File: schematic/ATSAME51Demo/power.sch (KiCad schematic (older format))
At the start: 37 parts, among them IC2 AZ1117IH-3.3TRG1, J1 Barrel_Jack_Switch, J2 Power, J3 Conn_01x02, J4 USB_B_Micro, J5 USB_B_Mini, J6 Conn_01x02, SW1 SW_MEC_5E, SW2 SW_MEC_5E, SW3 SW_MEC_5E

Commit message: Footprints assigned
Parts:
- D2, D5, D6, D7: footprint (none) -> LED_SMD:LED_0603_1608Metric
- IC2: footprint SOT230P700X180-4N -> SamacSys_Parts:SOT230P700X180-4N
- J2: footprint (none) -> Connector_PinHeader_2.54mm:PinHeader_2x03_P2.54mm_Vertical
- J3, J6: footprint (none) -> Connector_PinHeader_2.54mm:PinHeader_1x02_P2.54mm_Vertical
- R1, R5, R6, R7, R8: footprint (none) -> Resistor_SMD:R_0603_1608Metric
- SW1: footprint (none) -> SamacSys_Parts:PTS647SK38SMTR2LFS
- SW2, SW3: footprint (none) -> SamacSys_Parts:FSM16JH
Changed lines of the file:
@@
 F 0 "IC2" H 3800 885 50  0000 C CNN
 F 1 "AZ1117IH-3.3TRG1" H 3800 976 50  0000 C CNN
-F 2 "SOT230P700X180-4N" H 4300 1450 50  0001 L CNN
+F 2 "SamacSys_Parts:SOT230P700X180-4N" H 4300 1450 50  0001 L CNN
 F 3 "" H 4300 1350 50  0001 L CNN
 F 4 "LDO Voltage Regulators LDO BJT HiCurr 1.35A 10Hz to 10KHz" H 4300 1250 50  0001 L CNN "Description"
@@
 F 0 "SW1" H 2150 7143 50  0000 C CNN
 F 1 "SW_MEC_5E" H 2150 7144 50  0001 C CNN
-F 2 "" H 2150 7150 50  0001 C CNN
+F 2 "SamacSys_Parts:PTS647SK38SMTR2LFS" H 2150 7150 50  0001 C CNN
 F 3 "http://www.apem.com/int/index.php?controller=attachment&id_attachment=1371" H 2150 7150 50  0001 C CNN
 	1    2150 6850
@@
 F 0 "SW2" H 3250 7143 50  0000 C CNN
 F 1 "SW_MEC_5E" H 3250 7144 50  0001 C CNN
-F 2 "" H 3250 7150 50  0001 C CNN
+F 2 "SamacSys_Parts:FSM16JH" H 3250 7150 50  0001 C CNN
 F 3 "http://www.apem.com/int/index.php?controller=attachment&id_attachment=1371" H 3250 7150 50  0001 C CNN
 	1    3250 6850
@@
 F 0 "SW3" H 4350 7143 50  0000 C CNN
 F 1 "SW_MEC_5E" H 4350 7144 50  0001 C CNN
-F 2 "" H 4350 7150 50  0001 C CNN
+F 2 "SamacSys_Parts:FSM16JH" H 4350 7150 50  0001 C CNN
 F 3 "http://www.apem.com/int/index.php?controller=attachment&id_attachment=1371" H 4350 7150 50  0001 C CNN
 	1    4350 6850
@@
 F 0 "D2" H 7393 4767 50  0000 C CNN
 F 1 "Red" H 7393 4676 50  0000 C CNN
-F 2 "" H 7400 4550 50  0001 C CNN
+F 2 "LED_SMD:LED_0603_1608Metric" H 7400 4550 50  0001 C CNN
 F 3 "~" H 7400 4550 50  0001 C CNN
 	1    7400 4550
@@
 F 0 "D5" H 7793 4767 50  0000 C CNN
 F 1 "Yellow" H 7793 4676 50  0000 C CNN
-F 2 "" H 7800 4550 50  0001 C CNN
+F 2 "LED_SMD:LED_0603_1608Metric" H 7800 4550 50  0001 C CNN
 F 3 "~" H 7800 4550 50  0001 C CNN
 	1    7800 4550
@@
 F 0 "D6" H 8193 4767 50  0000 C CNN
 F 1 "Blue" H 8193 4676 50  0000 C CNN
-F 2 "" H 8200 4550 50  0001 C CNN
+F 2 "LED_SMD:LED_0603_1608Metric" H 8200 4550 50  0001 C CNN
 F 3 "~" H 8200 4550 50  0001 C CNN
 	1    8200 4550
@@
 F 0 "D7" H 8593 4767 50  0000 C CNN
 F 1 "Green" H 8593 4676 50  0000 C CNN
-F 2 "" H 8600 4550 50  0001 C CNN
+F 2 "LED_SMD:LED_0603_1608Metric" H 8600 4550 50  0001 C CNN
 F 3 "~" H 8600 4550 50  0001 C CNN
 	1    8600 4550
@@
 F 0 "R5" H 7470 4996 50  0000 L CNN
 F 1 "220R" H 7470 4905 50  0000 L CNN
-F 2 "" V 7330 4950 50  0001 C CNN
+F 2 "Resistor_SMD:R_0603_1608Metric" V 7330 4950 50  0001 C CNN
 F 3 "~" H 7400 4950 50  0001 C CNN
 	1    7400 4950
@@
 F 0 "R6" H 7870 4996 50  0000 L CNN
 F 1 "220R" H 7870 4905 50  0000 L CNN
-F 2 "" V 7730 4950 50  0001 C CNN
+F 2 "Resistor_SMD:R_0603_1608Metric" V 7730 4950 50  0001 C CNN
 F 3 "~" H 7800 4950 50  0001 C CNN
 	1    7800 4950
@@
 F 0 "R7" H 8270 4996 50  0000 L CNN
 F 1 "220R" H 8270 4905 50  0000 L CNN
-F 2 "" V 8130 4950 50  0001 C CNN
+F 2 "Resistor_SMD:R_0603_1608Metric" V 8130 4950 50  0001 C CNN
 F 3 "~" H 8200 4950 50  0001 C CNN
 	1    8200 4950
@@
 F 0 "R8" H 8670 4996 50  0000 L CNN
 F 1 "220R" H 8670 4905 50  0000 L CNN
-F 2 "" V 8530 4950 50  0001 C CNN
+F 2 "Resistor_SMD:R_0603_1608Metric" V 8530 4950 50  0001 C CNN
 F 3 "~" H 8600 4950 50  0001 C CNN
 	1    8600 4950
@@
 F 0 "J3" H 7480 5542 50  0000 L CNN
 F 1 "Conn_01x02" H 7480 5451 50  0001 L CNN
-F 2 "" H 7400 5550 50  0001 C CNN
+F 2 "Connector_PinHeader_2.54mm:PinHeader_1x02_P2.54mm_Vertical" H 7400 5550 50  0001 C CNN
 F 3 "~" H 7400 5550 50  0001 C CNN
 	1    7400 5550
@@
 F 0 "J6" H 8680 5442 50  0000 L CNN
 F 1 "Conn_01x02" H 8680 5351 50  0001 L CNN
-F 2 "" H 8600 5450 50  0001 C CNN
+F 2 "Connector_PinHeader_2.54mm:PinHeader_1x02_P2.54mm_Vertical" H 8600 5450 50  0001 C CNN
 F 3 "~" H 8600 5450 50  0001 C CNN
 	1    8600 5450
@@
 F 0 "R1" H 1670 6596 50  0000 L CNN
 F 1 "100k" H 1670 6505 50  0000 L CNN
-F 2 "" V 1530 6550 50  0001 C CNN
+F 2 "Resistor_SMD:R_0603_1608Metric" V 1530 6550 50  0001 C CNN
 F 3 "~" H 1600 6550 50  0001 C CNN
 	1    1600 6550
@@
 F 0 "J2" H 1850 3367 50  0000 C CNN
 F 1 "Power" H 1850 3276 50  0000 C CNN
-F 2 "" H 1800 3050 50  0001 C CNN
+F 2 "Connector_PinHeader_2.54mm:PinHeader_2x03_P2.54mm_Vertical" H 1800 3050 50  0001 C CNN
 F 3 "~" H 1800 3050 50  0001 C CNN
 	1    1800 3050

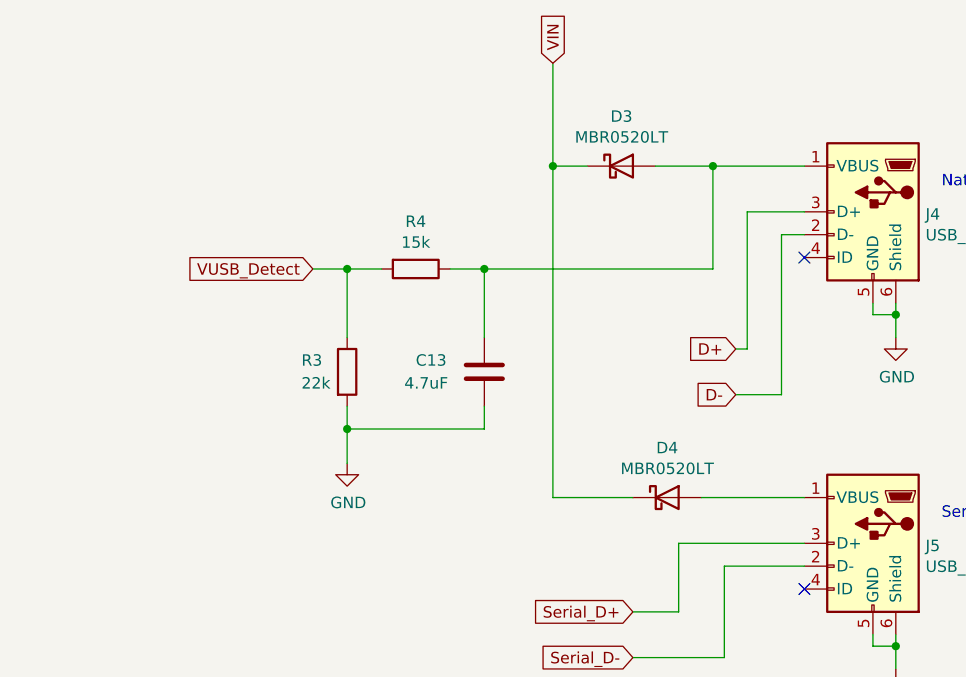
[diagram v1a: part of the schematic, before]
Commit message: Removed USB detect
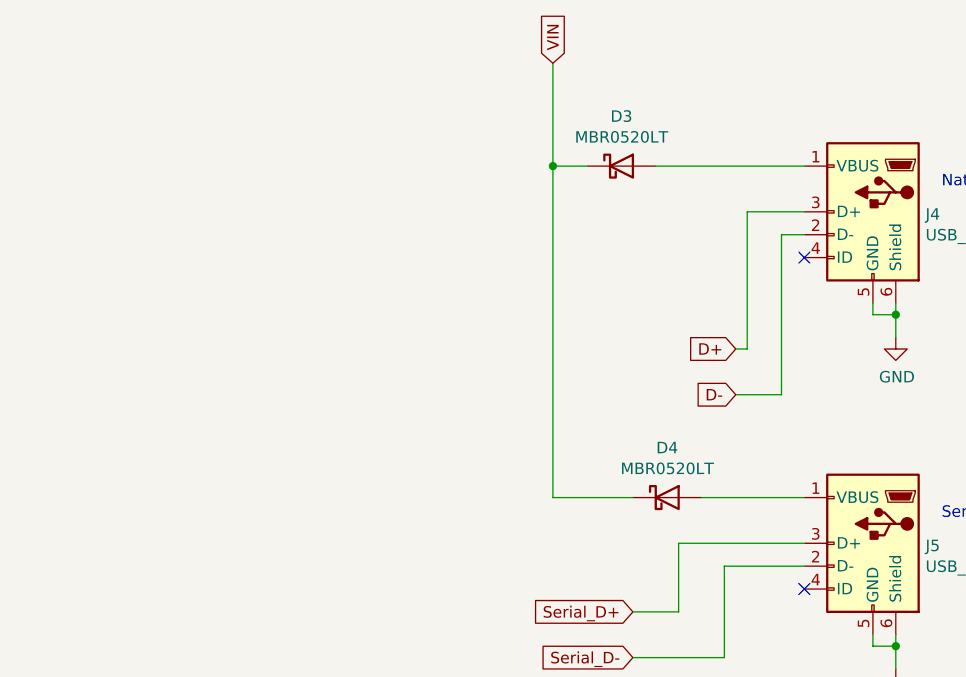
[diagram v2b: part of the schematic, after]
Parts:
- removed C13: 4.7uF, Capacitor_SMD:C_0603_1608Metric, symbol Device:C
- removed R3: 22k, Resistor_SMD:R_0603_1608Metric, symbol Device:R
- removed R4: 15k, Resistor_SMD:R_0603_1608Metric, symbol Device:R
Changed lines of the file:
@@
 encoding utf-8
 Sheet 2 3
-Title "SAMduino"
-Date "2021-10-22"
+Title "ATSAME51 Demo Board"
+Date "2021-10-25"
 Rev "1.0"
 Comp "Quantum Embedded Systems"
@@
 Wire Wire Line
 	2950 1250 2950 1650
-$Comp
-L Device:R R4
-U 1 1 61628FE0
-P 6600 1650
-F 0 "R4" V 6393 1650 50  0000 C CNN
-F 1 "15k" V 6484 1650 50  0000 C CNN
-F 2 "Resistor_SMD:R_0603_1608Metric" V 6530 1650 50  0001 C CNN
-F 3 "~" H 6600 1650 50  0001 C CNN
-	1    6600 1650
-	0    1    1    0
-$EndComp
-$Comp
-L Device:R R3
-U 1 1 61629740
-P 6300 2100
-F 0 "R3" H 6100 2150 50  0000 L CNN
-F 1 "22k" H 6100 2050 50  0000 L CNN
-F 2 "Resistor_SMD:R_0603_1608Metric" V 6230 2100 50  0001 C CNN
-F 3 "~" H 6300 2100 50  0001 C CNN
-	1    6300 2100
-	1    0    0    -1
-$EndComp
-$Comp
-L Device:C C13
-U 1 1 61629C96
-P 6900 2100
-F 0 "C13" H 6600 2150 50  0000 L CNN
-F 1 "4.7uF" H 6550 2050 50  0000 L CNN
-F 2 "Capacitor_SMD:C_0603_1608Metric" H 6938 1950 50  0001 C CNN
-F 3 "~" H 6900 2100 50  0001 C CNN
-	1    6900 2100
-	1    0    0    -1
-$EndComp
-$Comp
-L power:GND #PWR024
-U 1 1 6162A7ED
-P 6300 2500
-F 0 "#PWR024" H 6300 2250 50  0001 C CNN
-F 1 "GND" H 6305 2327 50  0000 C CNN
-F 2 "" H 6300 2500 50  0001 C CNN
-F 3 "" H 6300 2500 50  0001 C CNN
-	1    6300 2500
-	1    0    0    -1
-$EndComp
-Wire Wire Line
-	6750 1650 6900 1650
-Wire Wire Line
-	6900 1950 6900 1650
-Wire Wire Line
-	6300 2250 6300 2350
-Wire Wire Line
-	6900 2250 6900 2350
-Wire Wire Line
-	6900 2350 6300 2350
-Connection ~ 6300 2350
-Wire Wire Line
-	6300 2350 6300 2500
-Wire Wire Line
-	6300 1950 6300 1650
-Wire Wire Line
-	6300 1650 6450 1650
-Text GLabel 6150 1650 0    50   Input ~ 0
-VUSB_Detect
 Text GLabel 7550 3150 0    50   Input ~ 0
 Serial_D+
@@
 Wire Wire Line
 	8000 2200 8200 2200
-Wire Wire Line
-	6900 1650 7900 1650
-Wire Wire Line
-	7900 1650 7900 1200
-Connection ~ 6900 1650
-Connection ~ 7900 1200
-Wire Wire Line
-	7900 1200 8300 1200
 $Comp
 L Device:C C4
@@
 VIN
 Connection ~ 3000 4500
-Wire Wire Line
-	6300 1650 6150 1650
-Connection ~ 6300 1650
 Text Notes 4000 2100 0    50   ~ 0
 3.3V Power\n1 A
@@
 Wire Wire Line
 	7200 750  7200 1200
-Wire Wire Line
-	7650 1200 7900 1200
 Wire Wire Line
 	7350 1200 7200 1200
@@
 Wire Wire Line
 	8600 4400 8600 4250
+Wire Wire Line
+	7650 1200 8300 1200
 $EndSCHEMATC

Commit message: Added  USB_VBUS_SENSE
And other minor improvements
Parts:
- added J17: Conn_01x02, Connector_PinHeader_2.54mm:PinHeader_1x02_P2.54mm_Vertical, symbol Connector_Generic:Conn_01x02
- added R3: 15k, Resistor_SMD:R_0603_1608Metric, symbol Device:R
- added R4: 22k, Resistor_SMD:R_0603_1608Metric, symbol Device:R
- R7: value 220R -> 62R
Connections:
- net GND: now also R4.2
- net at D3.2 (A), J4.1 (VBUS): now also R3.1
- new net: J17.2 (Pin_2), R3.2, R4.1
- new net PB17: J17.1 (Pin_1)
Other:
- note added: "USB_VBUS_SENSE enable"
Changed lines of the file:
@@
 AR Path="/6175619B/617D32DE" Ref="R7"  Part="1"
 F 0 "R7" H 8270 4996 50  0000 L CNN
-F 1 "220R" H 8270 4905 50  0000 L CNN
+F 1 "62R" H 8270 4905 50  0000 L CNN
 F 2 "Resistor_SMD:R_0603_1608Metric" V 8130 4950 50  0001 C CNN
 F 3 "~" H 8200 4950 50  0001 C CNN
@@
 	8600 4400 8600 4250
 Wire Wire Line
-	7650 1200 8300 1200
+	7650 1200 7850 1200
+$Comp
+L Device:R R3
+U 1 1 6190EC94
+P 6700 1700
+F 0 "R3" H 6770 1746 50  0000 L CNN
+F 1 "15k" H 6770 1655 50  0000 L CNN
+F 2 "Resistor_SMD:R_0603_1608Metric" V 6630 1700 50  0001 C CNN
+F 3 "~" H 6700 1700 50  0001 C CNN
+	1    6700 1700
+	1    0    0    -1
+$EndComp
+$Comp
+L Device:R R4
+U 1 1 6190F315
+P 6700 2200
+F 0 "R4" H 6770 2246 50  0000 L CNN
+F 1 "22k" H 6770 2155 50  0000 L CNN
+F 2 "Resistor_SMD:R_0603_1608Metric" V 6630 2200 50  0001 C CNN
+F 3 "~" H 6700 2200 50  0001 C CNN
+	1    6700 2200
+	1    0    0    -1
+$EndComp
+$Comp
+L Connector_Generic:Conn_01x02 J17
+U 1 1 6190FCD1
+P 6000 2000
+F 0 "J17" H 6000 1700 50  0000 C CNN
+F 1 "Conn_01x02" H 5918 1766 50  0001 C CNN
+F 2 "Connector_PinHeader_2.54mm:PinHeader_1x02_P2.54mm_Vertical" H 6000 2000 50  0001 C CNN
+F 3 "~" H 6000 2000 50  0001 C CNN
+	1    6000 2000
+	-1   0    0    1
+$EndComp
+Wire Wire Line
+	6700 1550 6700 1450
+Wire Wire Line
+	6700 1450 7850 1450
+Wire Wire Line
+	7850 1450 7850 1200
+Connection ~ 7850 1200
+Wire Wire Line
+	7850 1200 8300 1200
+Wire Wire Line
+	6700 1850 6700 1900
+$Comp
+L power:GND #PWR024
+U 1 1 61919F35
+P 6700 2350
+F 0 "#PWR024" H 6700 2100 50  0001 C CNN
+F 1 "GND" H 6705 2177 50  0000 C CNN
+F 2 "" H 6700 2350 50  0001 C CNN
+F 3 "" H 6700 2350 50  0001 C CNN
+	1    6700 2350
+	1    0    0    -1
+$EndComp
+Wire Wire Line
+	6200 1900 6700 1900
+Connection ~ 6700 1900
+Wire Wire Line
+	6700 1900 6700 2050
+Text GLabel 6200 2250 3    50   Input ~ 0
+PB17
+Wire Wire Line
+	6200 2250 6200 2000
+Text Notes 5550 1600 0    50   ~ 0
+USB_VBUS_SENSE enable
 $EndSCHEMATC

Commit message: Changed leds to 0805
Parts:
- D2, D5, D6, D7: footprint LED_SMD:LED_0603_1608Metric -> LED_SMD:LED_0805_2012Metric
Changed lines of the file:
@@
 F 0 "D2" H 7393 4767 50  0000 C CNN
 F 1 "Red" H 7393 4676 50  0000 C CNN
-F 2 "LED_SMD:LED_0603_1608Metric" H 7400 4550 50  0001 C CNN
+F 2 "LED_SMD:LED_0805_2012Metric" H 7400 4550 50  0001 C CNN
 F 3 "~" H 7400 4550 50  0001 C CNN
 	1    7400 4550
@@
 F 0 "D5" H 7793 4767 50  0000 C CNN
 F 1 "Yellow" H 7793 4676 50  0000 C CNN
-F 2 "LED_SMD:LED_0603_1608Metric" H 7800 4550 50  0001 C CNN
+F 2 "LED_SMD:LED_0805_2012Metric" H 7800 4550 50  0001 C CNN
 F 3 "~" H 7800 4550 50  0001 C CNN
 	1    7800 4550
@@
 F 0 "D6" H 8193 4767 50  0000 C CNN
 F 1 "Blue" H 8193 4676 50  0000 C CNN
-F 2 "LED_SMD:LED_0603_1608Metric" H 8200 4550 50  0001 C CNN
+F 2 "LED_SMD:LED_0805_2012Metric" H 8200 4550 50  0001 C CNN
 F 3 "~" H 8200 4550 50  0001 C CNN
 	1    8200 4550
@@
 F 0 "D7" H 8593 4767 50  0000 C CNN
 F 1 "Green" H 8593 4676 50  0000 C CNN
-F 2 "LED_SMD:LED_0603_1608Metric" H 8600 4550 50  0001 C CNN
+F 2 "LED_SMD:LED_0805_2012Metric" H 8600 4550 50  0001 C CNN
 F 3 "~" H 8600 4550 50  0001 C CNN
 	1    8600 4550
